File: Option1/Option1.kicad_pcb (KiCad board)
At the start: 2 copper layers, 85 x 76.5 mm, 131 parts, among them J1501 GH-13AB, J1801 Conn_01x08_Socket, J401 Conn_01x05_Pin, J402 Conn_01x04_Pin, J403 Conn_01x05_Pin, J503 KF2EDGKRG-3.5-2*7P, J999 Phoenix_Connetor_07x2pin_toWi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, Q1001 JY2302, Q1101 JY2302, Q1401 BC817-40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

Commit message: BOM und Positionsdaten korrigiert
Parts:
- renumbered USB to J1401, 3V3D to LED3V3D1
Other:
- board text added: "3V3D"
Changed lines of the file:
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@@
 		(layer "F.Cu")
 		(at 102.145 70.2 -90)
-		(property "Reference" "3V3D"
-			(at -2.625 -0.75 180)
+		(property "Reference" "LED3V3D1"
+			(at -2.625 -0.75 0)
 			(layer "F.SilkS")
+			(hide yes)
 			(effects
 				(font
@@
 		)
 		(property "Value" "Conn_01x05_Pin"
-			(at 0 12.54 270)
+			(at 0 12.54 90)
 			(layer "F.Fab")
 			(effects
@@
 		)
 		(property "Datasheet" ""
-			(at 0 0 270)
+			(at 0 0 90)
 			(layer "F.Fab")
 			(hide yes)
@@
 		)
 		(property "Description" "Generic connector, single row, 01x05, script generated"
-			(at 0 0 270)
+			(at 0 0 90)
 			(layer "F.Fab")
 			(hide yes)
@@
 		(sheetname "/Funk Reciever/")
 		(sheetfile "radio_reciever.kicad_sch")
-		(attr through_hole)
+		(attr through_hole exclude_from_pos_files exclude_from_bom dnp)
 		(fp_line
 			(start -1.2 11.4)
@@
 		(sheetname "/Funk Reciever/")
 		(sheetfile "radio_reciever.kicad_sch")
-		(attr through_hole)
+		(attr through_hole exclude_from_pos_files exclude_from_bom dnp)
 		(fp_line
 			(start -1.2 11.4)
@@
 		(sheetname "/RFID Antenne/")
 		(sheetfile "RFID.kicad_sch")
-		(attr through_hole)
+		(attr through_hole exclude_from_pos_files exclude_from_bom dnp)
 		(fp_line
 			(start -1.38 19.16)
@@
 		(layer "F.Cu")
 		(at 181.5875 86.8 90)
-		(property "Reference" "USB"
+		(property "Reference" "J1401"
 			(at -5.32 2.5125 0)
 			(layer "F.SilkS")
+			(hide yes)
 			(effects
 				(font
@@
 		(sheetname "/Funk Reciever/")
 		(sheetfile "radio_reciever.kicad_sch")
-		(attr through_hole)
+		(attr through_hole exclude_from_pos_files exclude_from_bom dnp)
 		(fp_line
 			(start -1.2 -1.2)
@@
 		)
 	)
+	(gr_text "3V3D"
+		(at 103.14 67.69 0)
+		(layer "F.SilkS")
+		(effects
+			(font
+				(size 1 1)
+				(thickness 0.15)
+			)
+		)
+	)

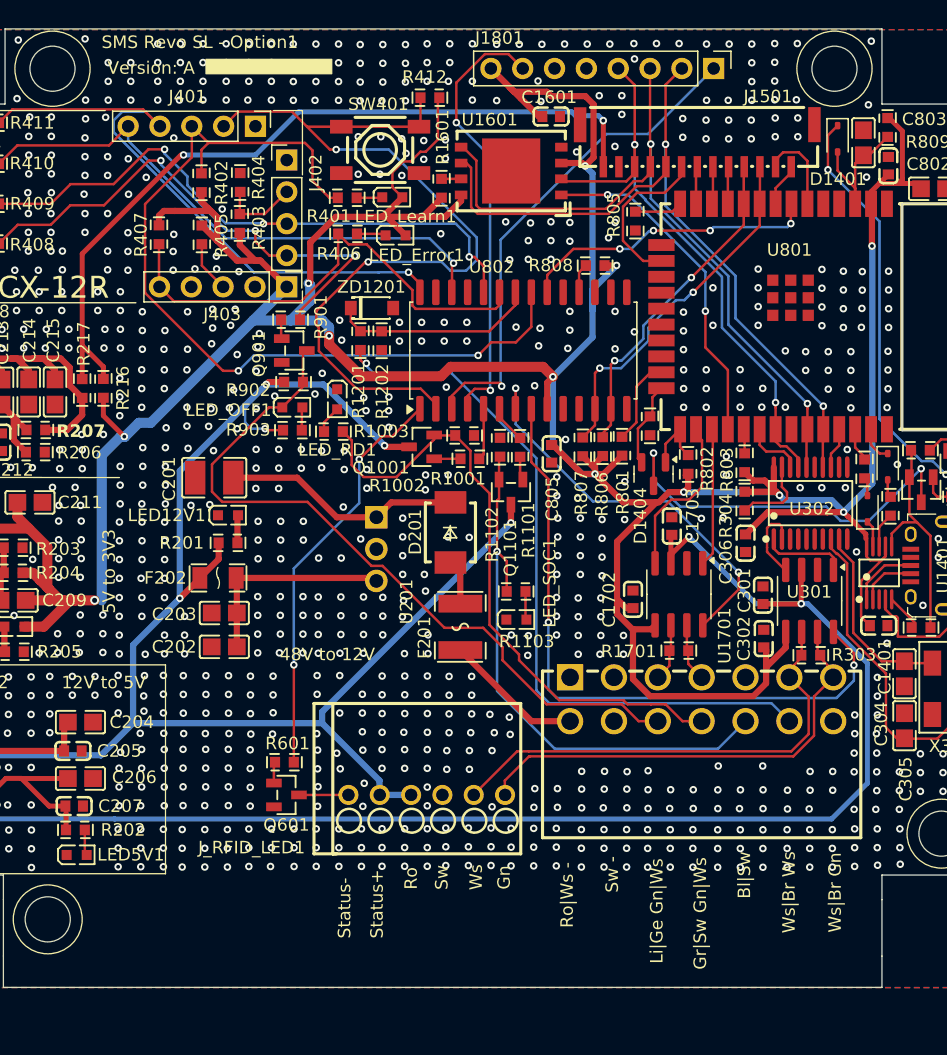
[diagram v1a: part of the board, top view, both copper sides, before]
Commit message: Programming Header hinzugefügt für flashen via DevKit
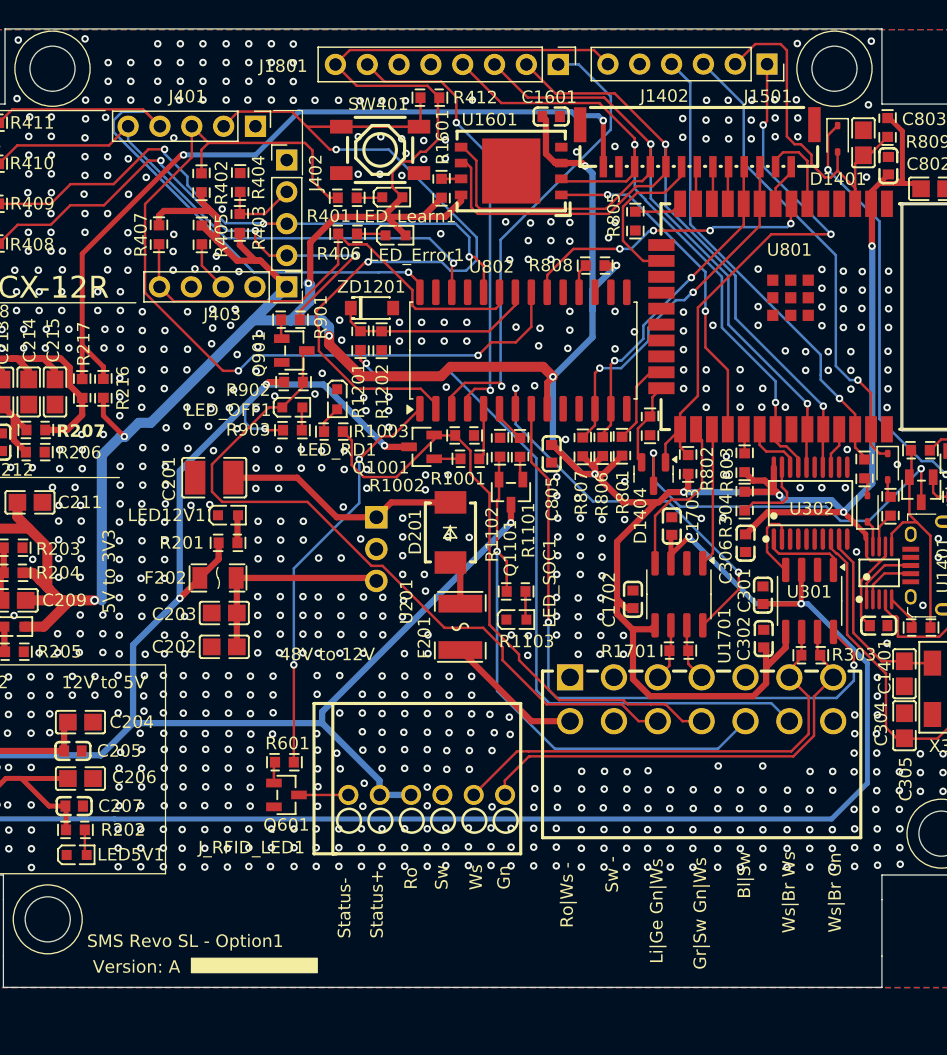
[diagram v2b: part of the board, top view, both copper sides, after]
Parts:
- added J1402: Conn_01x06_Pin, Connector_PinSocket_2.54mm:PinSocket_1x06_P2.54mm_Vertical, F.Cu at (168.8, 46.8)
- moved J1801 12.4 mm to (152.1, 46.8)
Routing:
- net IO0: track 5.43 -> 44.7 mm, vias 0 -> 2
- net IO22: track 2.83 -> 38.0 mm, vias 0 -> 1
- net IO23: track 2.86 -> 37.9 mm, vias 0 -> 1
- net 3.3V: track 349.9 -> 368.5 mm
- net /MCT  Wlan/ESP_EN: track 11.5 -> 29.4 mm
- net IO19: track 46.8 -> 56.8 mm
- net IO21: track 60.2 -> 69.2 mm
- net IO3: track 61.3 -> 68.4 mm
- net /MCT  Wlan/SPI_CS_RFID: track 40.0 -> 37.7 mm
- net GND: vias 868 -> 816
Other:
- board text added: "Programming Header"

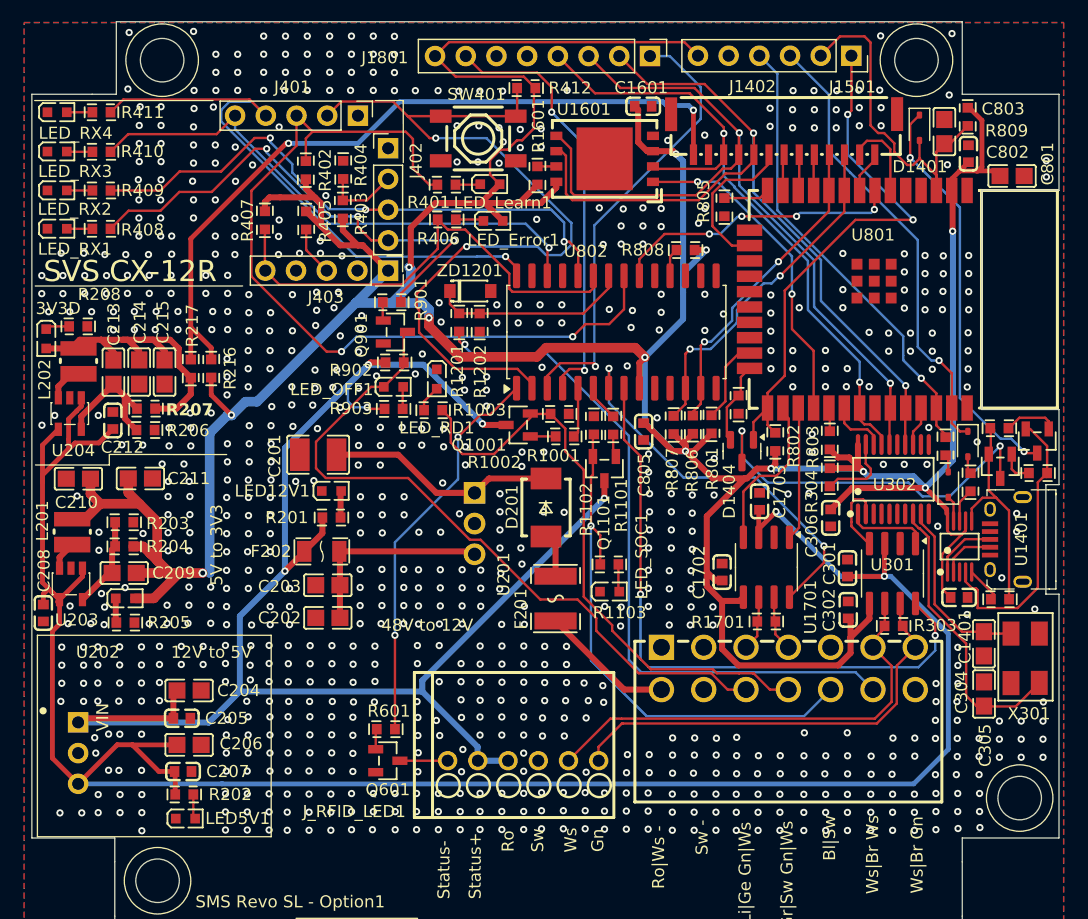
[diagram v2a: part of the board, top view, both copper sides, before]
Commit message: Platine korrigeiert, 5V DCDC getauscht, 3.3V Display Versorgung entfernt. Bauteile neu angeordnet, USB 5V auf 5V Supply geführt
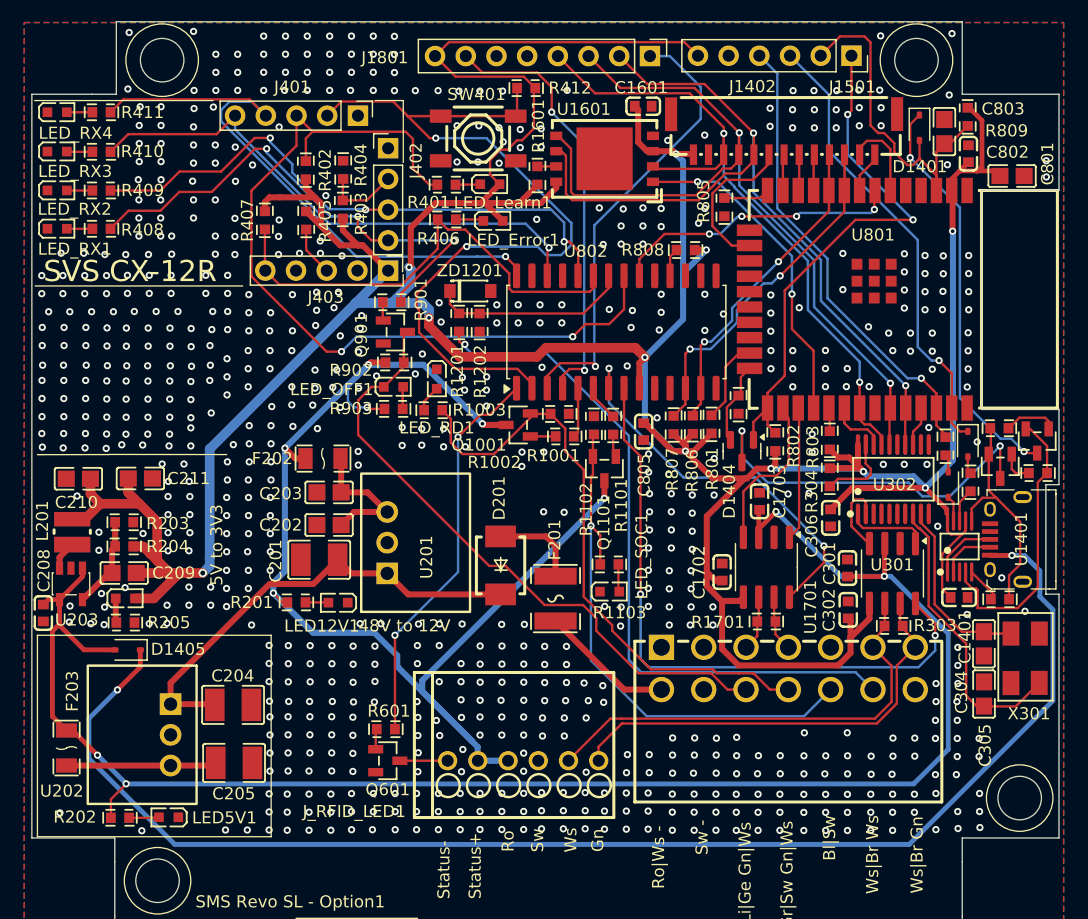
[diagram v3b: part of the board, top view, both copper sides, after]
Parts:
- removed C206: 10uF / 25V, easyeda2kicad:C0805
- removed C207: 100nF / 25V, easyeda2kicad:C0603
- removed C212: 22uF / 6.3V, easyeda2kicad:C0603
- removed C213: 22pF, easyeda2kicad:C0805
- removed C214, C215: 22uF, easyeda2kicad:C0805
- removed L202: 2.2uH, easyeda2kicad:IND-SMD_L3.0-W3.0_NR3010
- removed LED3V3D1: XL-1608SYGC-06, easyeda2kicad:LED0603-RD_GREEN
- removed R206: 49.9k, easyeda2kicad:R0603
- removed R207: 220k, easyeda2kicad:R0603
- removed R208: 220Ω, easyeda2kicad:R0603
- removed R216, R217: 0Ω, easyeda2kicad:R0603
- removed U204: SY8089AAAC, easyeda2kicad:SOT-23-5_L3.0-W1.7-P0.95-LS2.8-BR
- added D1405: 1N5819WS, Diode_SMD:D_SOD-323, F.Cu at (108.9, 95.9)
- added F203: JK-NSMD075, easyeda2kicad:F1206, F.Cu at (103.8, 104.1)
- C204: value 10uF / 25V -> 10uF / 63V; footprint easyeda2kicad:C0805 -> easyeda2kicad:C1210
- C205: value 100nF / 25V -> 22uF / 10V; footprint easyeda2kicad:C0603 -> easyeda2kicad:C1210
- F201: value JK-MSMD020-60V -> JK-MSMD030-60V
- LED12V1: value XL-1608SYGC-06 -> XL-1608SYGC-12
- LED5V1: value XL-1608SYGC-06 -> XL-1608SYGC-5
- R203: value 49.9k -> 150k
- R204: value 220k -> 680k
- U202: value K7805-500R2_C909663 -> U7805-500; footprint easyeda2kicad:PWRM-TH_K78XX-500R3 -> easyeda2kicad:PWRM-TH_3P-L11.6-W9.0-P2.54
- moved LED12V1 9.26 mm to (126.3, 92.0), turned to 180 degrees
- moved C201 8.69 mm to (124.7, 88.5)
- moved U202 7.80 mm to (112.4, 103.0), turned to -90 degrees
- moved C202 7.68 mm to (125.5, 85.6)
- moved C203 7.68 mm to (125.5, 82.9)
- moved F202 7.68 mm to (125.0, 80.1)
- moved R201 7.60 mm to (122.8, 92.0)
- moved U201 7.40 mm to (130.4, 87.1), turned to 90 degrees
- moved D201 6.09 mm to (139.7, 89.0), turned to 90 degrees
- moved C205 5.68 mm to (117.7, 105.3), turned to 0 degrees
- moved R202 5.66 mm to (108.2, 109.8)
- moved C204 3.83 mm to (117.6, 100.5), turned to 0 degrees
- moved LED5V1 1.40 mm to (112.3, 109.8), turned to 180 degrees
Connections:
- C201 pad 1: /Powersupply/48V_FUSED -> 48V_Fused
- C204 pad 1: GND -> 48V_Fused
- C204 pad 2: 12V -> GND
- C205 pad 1: GND -> Net-(U202-Vout)
- C205 pad 2: 12V -> GND
- D201 pad 2: /Powersupply/48V_FUSED -> 48V_Fused
- J1501 pad 13: /Powersupply/3.3V_D -> 3.3V
- J1501 pad 14: unconnected-(J1501-Pad14) -> GND
- J1501 pad 15: unconnected-(J1501-Pad15) -> GND
- J401 pad 1: Sparmodus_enable -> GND
- U1601 pad 9: unconnected-(U1601-EP-Pad9) -> GND
- U201 pad 1: /Powersupply/48V_FUSED -> 48V_Fused
- U202 pad 1: 12V -> 48V_Fused
- U202 pad 3: 5V -> Net-(U202-Vout)
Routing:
- net /USB Port/VBUS: track 0.00 -> 114.2 mm, vias 0 -> 2
- net /Powersupply/3.3V_D: track 63.6 -> 0.00 mm, vias 2 -> 0
- net 48V_Fused: track 0.00 -> 38.1 mm
- net 5V: track 178.2 -> 140.1 mm, vias 2 -> 4
- net 12V: track 130.7 -> 101.4 mm, vias 5 -> 6
- net /Powersupply/3.3V_D1: track 26.7 -> 0.00 mm
- net /Powersupply/48V_FUSED: track 19.6 -> 0.00 mm
- net Net-(U202-Vout): track 0.00 -> 12.4 mm
- net Net-(U204-FB): track 11.1 -> 0.00 mm
- net /Notaus Schalter/Notaus_VCU: track 58.8 -> 52.2 mm
- net /Powersupply/12V_OUT: track 16.8 -> 11.6 mm
- net Net-(D201-A): track 3.61 -> 7.38 mm
- net 3.3V: track 368.5 -> 365.6 mm, vias 12 -> 11
- net Net-(U204-LX): track 2.46 -> 0.00 mm
- net Net-(LED3V3D1-K): track 1.99 -> 0.00 mm
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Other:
- board text removed: "12V to 5V"
- board text removed: "3V3D"

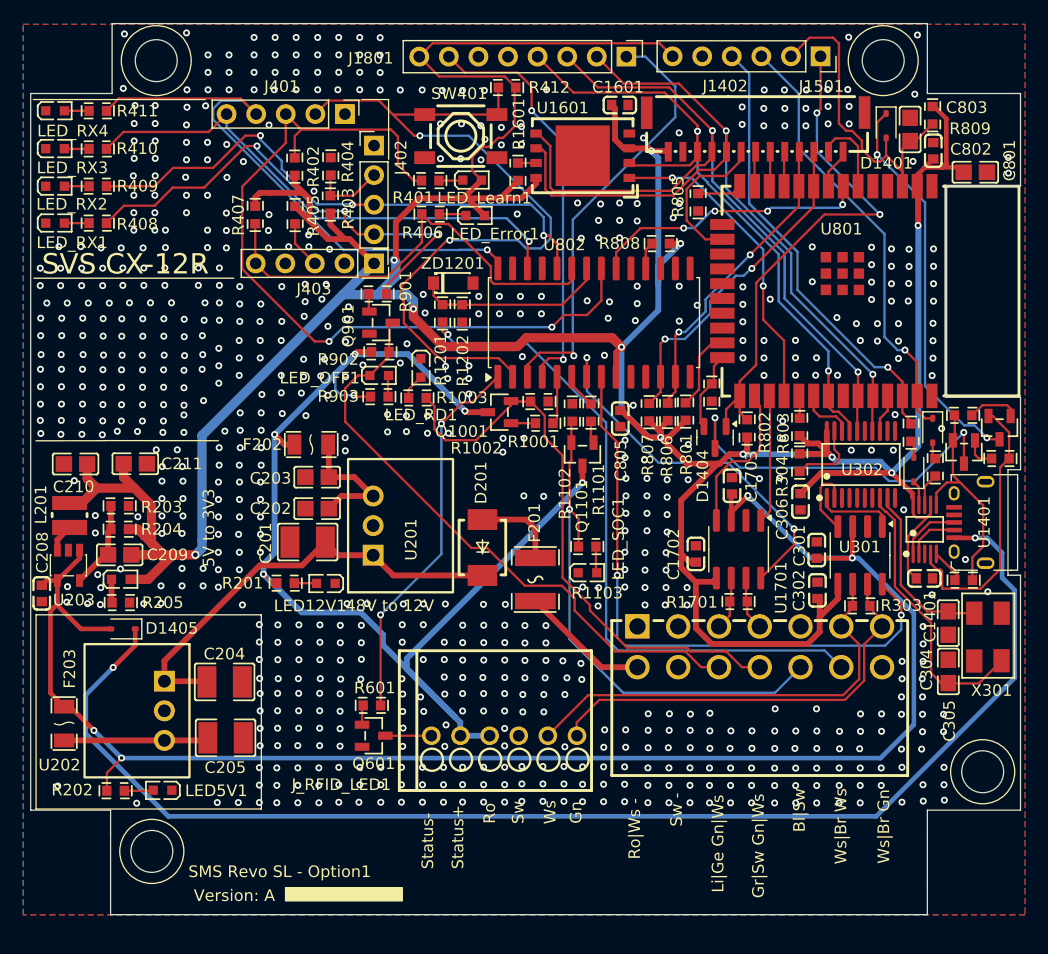
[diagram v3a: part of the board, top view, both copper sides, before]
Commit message: Kapitel 6 begonnen, Codeteile angepasst, GPIO Exp WriteBit korrigiert, Send SOC /RemoteDrive Delay entfernt
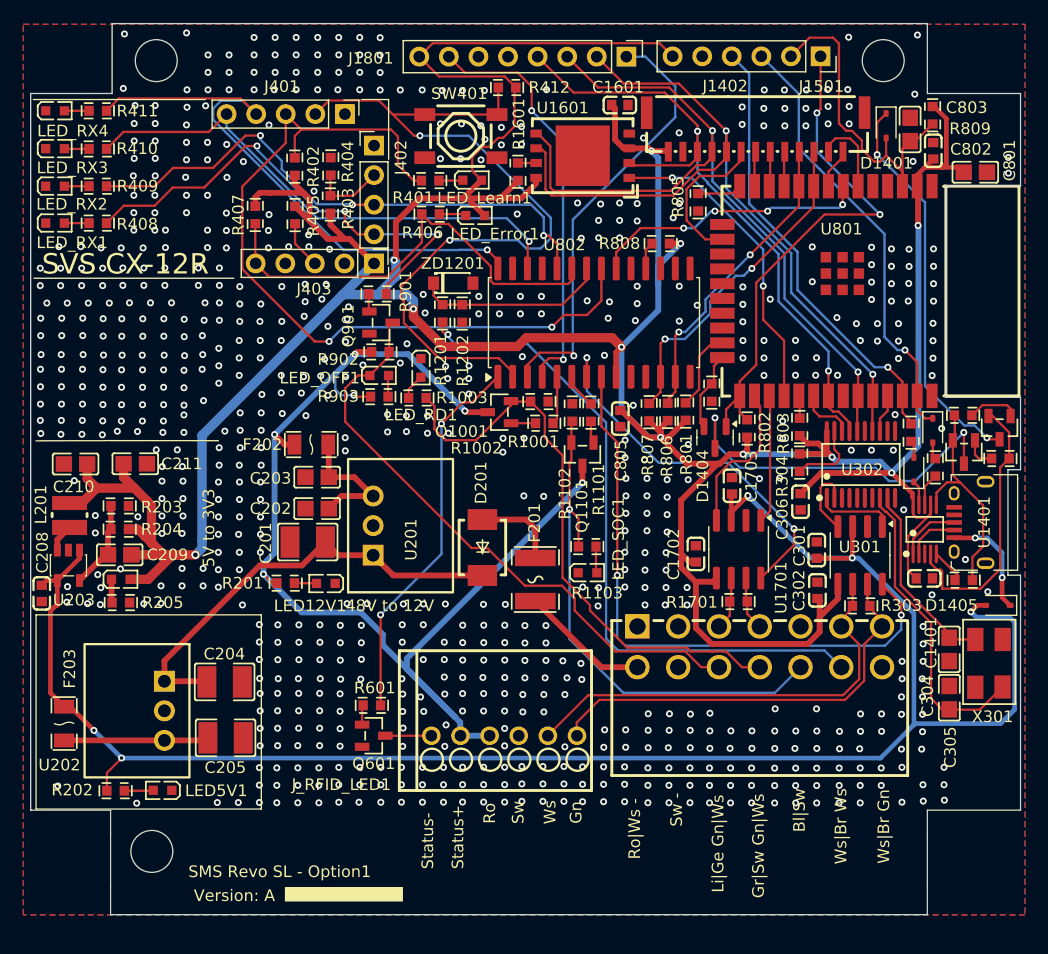
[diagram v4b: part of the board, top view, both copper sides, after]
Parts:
- moved D1405 75.1 mm to (184.0, 93.9)
- moved C304 2.26 mm to (179.8, 97.7)
- moved X301 2.26 mm to (183.3, 98.9)
- moved C305 2.26 mm to (179.8, 101.8)
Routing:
- net /USB Port/VBUS: track 114.2 -> 9.47 mm
- net 5V: track 140.1 -> 157.0 mm, vias 4 -> 5
- net Net-(U302-OSC2): track 24.1 -> 26.4 mm
- net Net-(U302-OSC1): track 15.3 -> 16.4 mm
- net GND: vias 732 -> 730
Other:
- outline, holes or cut-outs redrawn
